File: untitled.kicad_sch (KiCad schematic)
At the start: 11 parts, among them IC1 MAX11108AVB+T

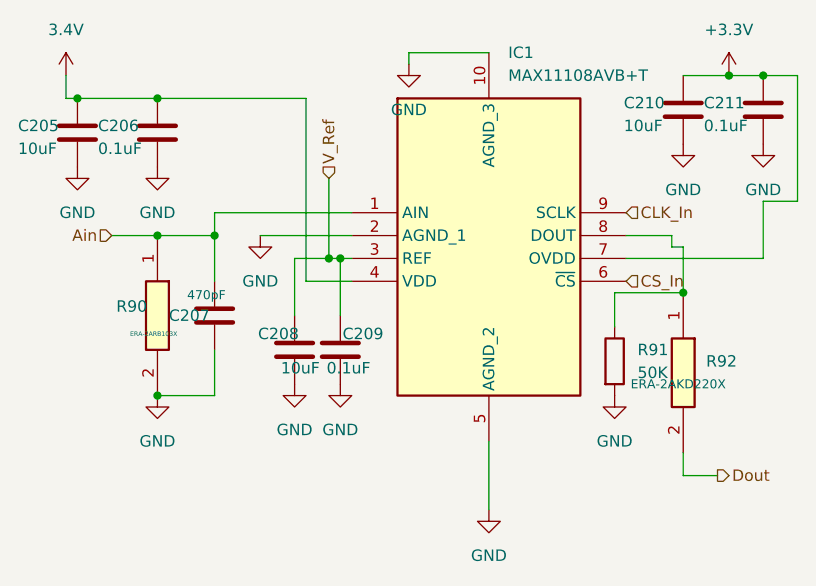
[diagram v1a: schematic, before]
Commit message: Updated schematic and PCB layout, no more precision Vrefs
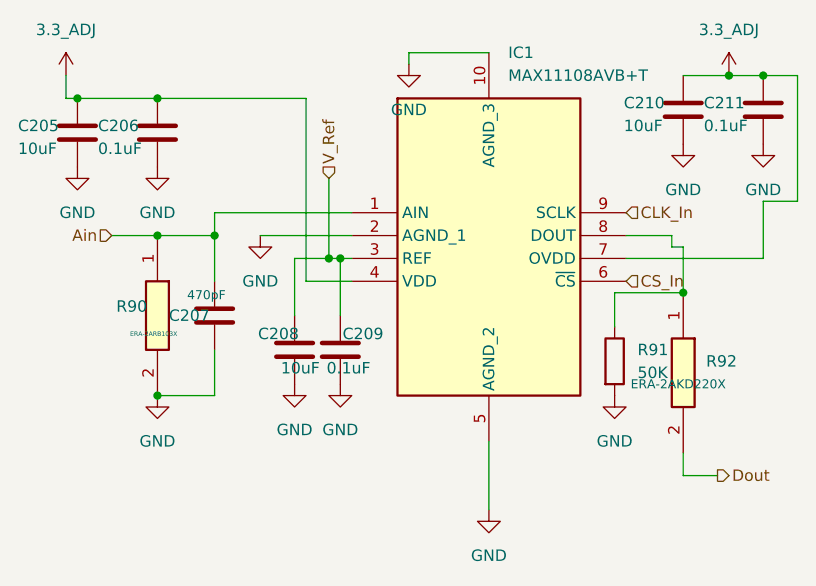
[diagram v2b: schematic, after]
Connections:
- net 3.4V is gone; now on net 3.3_ADJ: C205.1, C206.1, IC1.4 (VDD)
- net +3.3V renamed 3.3_ADJ
